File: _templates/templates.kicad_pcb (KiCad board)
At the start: 2 copper layers, 180.2 x 128.5 mm, 0 parts

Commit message: added some 3d models and backlog
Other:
- board size 180.2 x 128.5 mm -> 182.9 x 128.5 mm
- board text added: "Clandestine Circutry"

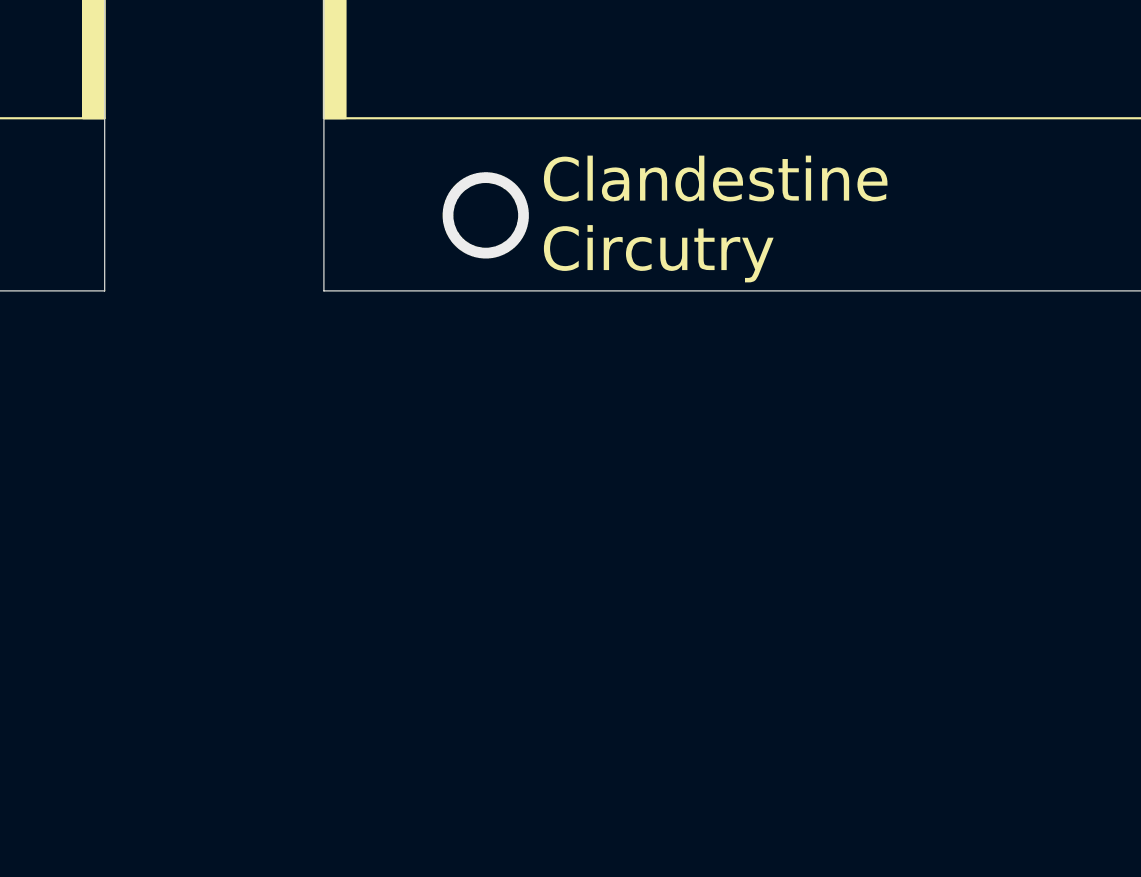
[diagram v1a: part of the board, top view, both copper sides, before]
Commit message: Marbles added
Beware! T_clock is shorted to ground. Fix before using this PCB
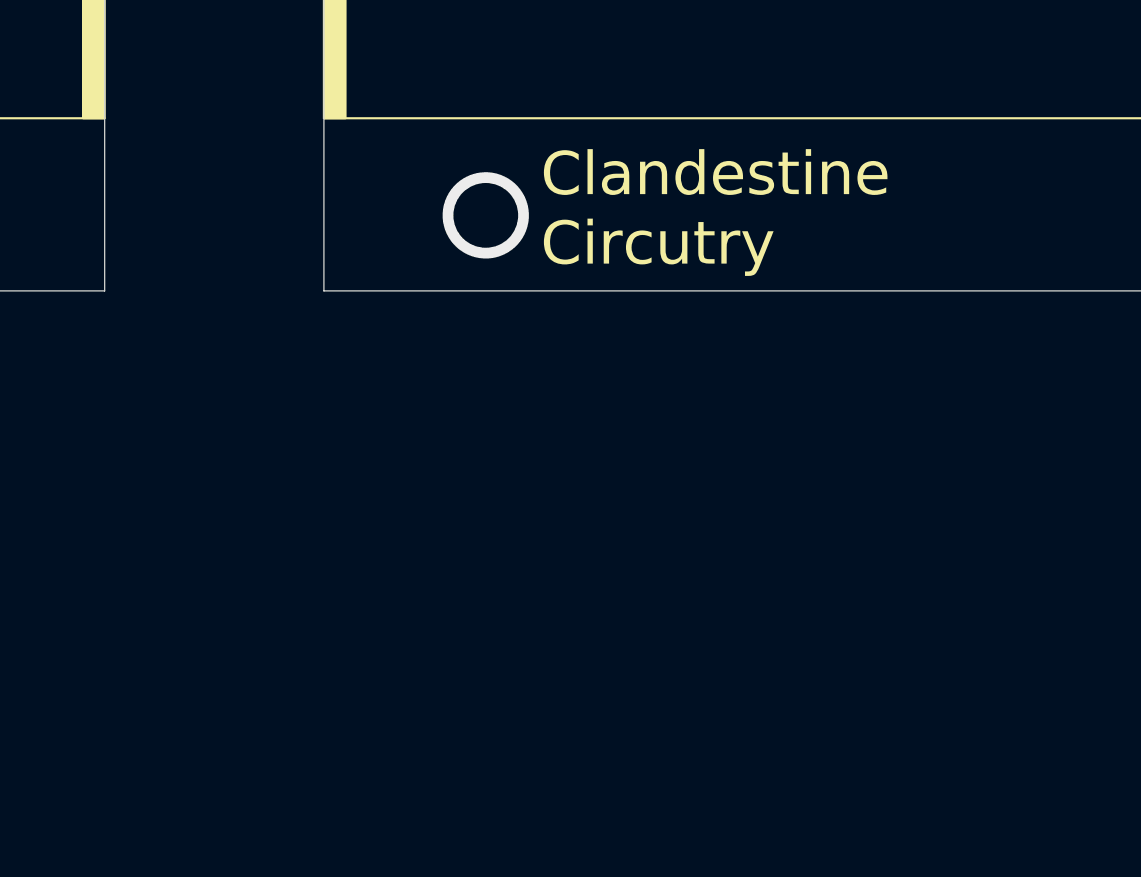
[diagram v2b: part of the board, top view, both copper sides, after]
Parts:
- added ?: , , F.Cu at (143.9, 183.0)
